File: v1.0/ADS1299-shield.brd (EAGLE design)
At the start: 63.5 x 25.4 mm, 77 parts, among them IC2 TPS72325DBVT, IC3 TPS73225DBVT, U1 ADS1299IPAG

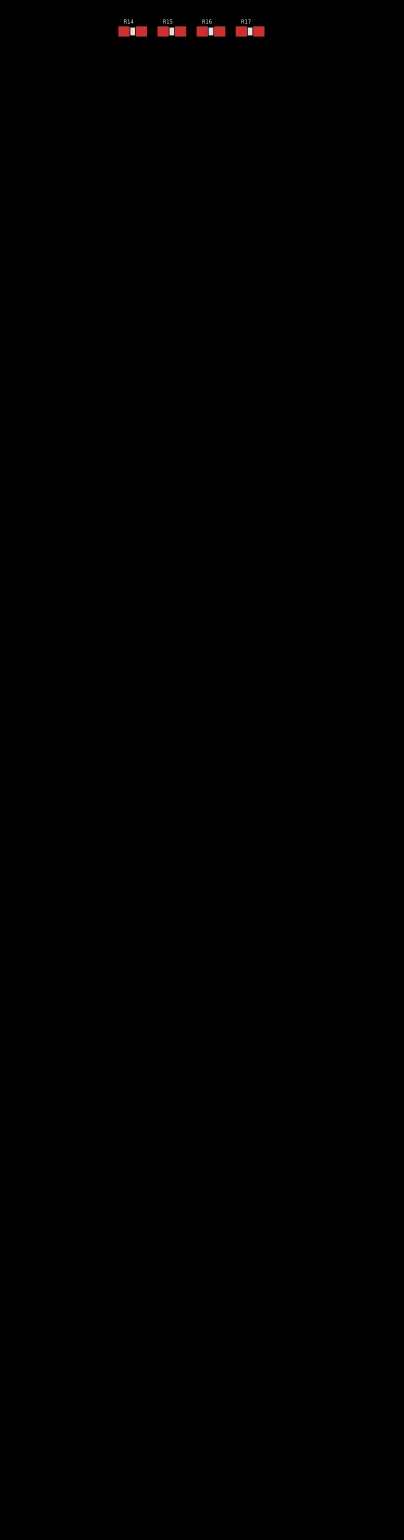
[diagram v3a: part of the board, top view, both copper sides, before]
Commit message: configuration jumpers added but not done; EEPROM in and finished; level shifters finished
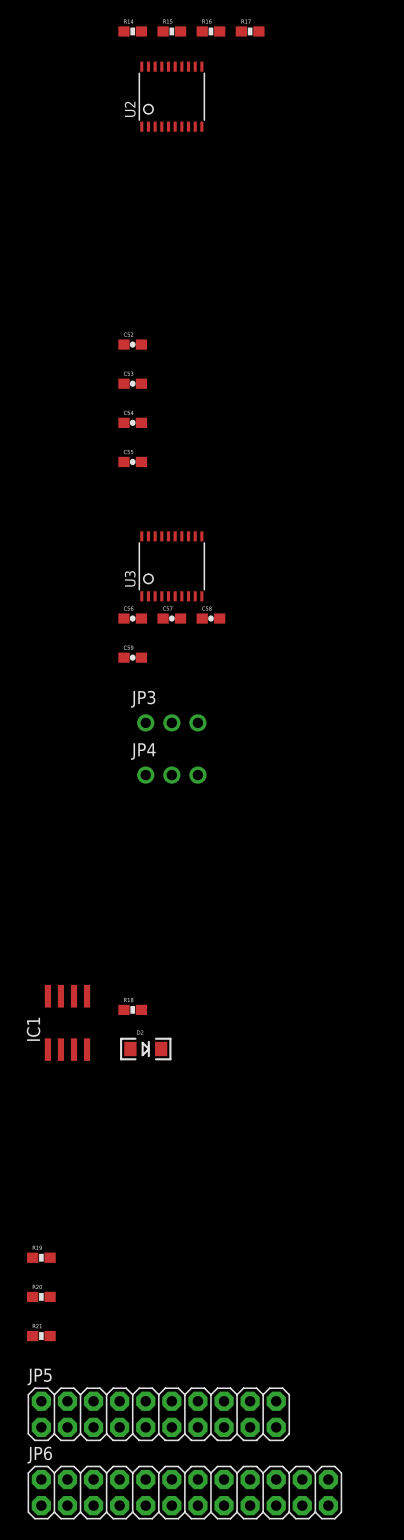
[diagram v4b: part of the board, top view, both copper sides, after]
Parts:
- added C52, C54, C56, C58: 1uF, SparkFun-Passives:0603-CAP
- added C53, C55, C57, C59: 0.1uF, SparkFun-Passives:0603-CAP
- added D2: RED, SparkFun-LED:LED-1206
- added IC1: 24AA256UID, microchip:SO-08
- added JP3, JP4: (no value), adafruit:1X03-CLEANBIG
- added JP5: (no value), pin-headers:2X10
- added JP6: (no value), pin-headers:2X12
- added R18: 270, SparkFun-Passives:0603-RES
- added R19, R20, R21: 10k, SparkFun-Passives:0603-RES
- added U2, U3: TXB0108PWR, adafruit:TSSOP20
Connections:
- removed net SPI_DRDY: U1.47
- removed net SPI_START: U1.38
- new net !ADS_PWDN: U2.12
- new net !ADS_RESET: U3.20
- new net !SPI_CS: U1.39
- new net ADS_CLK: U2.13
- new net ADS_CLKSEL: U2.14
- new net ADS_DRDY: U2.20
- new net ADS_SPI_CLK: U2.17
- new net ADS_SPI_CS: U2.18
- new net ADS_SPI_IN: U2.16
- new net ADS_SPI_OUT: U2.15
- new net ADS_START: U3.18
- new net ARD_UNUSED@1: U3.17
- new net ARD_UNUSED@2: U3.16
- new net ARD_UNUSED@3: U3.15
- new net ARD_UNUSED@4: U3.14
- new net ARD_UNUSED@5: U3.12, U3.13
- new net BOARD_ADDR_0: IC1.1, JP6.23, R19.2
- new net BOARD_ADDR_1: IC1.2, JP6.21, R20.2
- new net BOARD_ADDR_2: IC1.3, R21.2
- new net DRDY: U1.47, U2.1
- new net DVDD1: C56.2, C57.2, U3.2
- new net IOREF: C54.2, C55.2, U2.19
- new net IOREF1: C58.2, C59.2, U3.19
- new net N$14: D2.A, R18.2
- new net SCL1: IC1.6
- new net SDA1: IC1.5
- new net START: U1.38, U3.3
- new net UNUSED@1: U3.4
- new net UNUSED@2: U3.5
- new net UNUSED@3: U3.6, U3.7
- new net UNUSED@4: U3.8
- new net UNUSED@5: U3.9
- net !PWDN: now also U2.9
- net !RESET: now also U3.1
- net AGND: now also C52.1, C53.1, C54.1, C55.1, C56.1, C57.1, C58.1, C59.1, D2.C, IC1.4, IC1.7, R19.1, R20.1, R21.1, U2.11, U3.11
- net CLK: now also U2.8
- net CLKSEL: now also U2.7
- net DVDD: now also C52.2, C53.2, IC1.8, JP6.22, JP6.24, U2.2
- net GPIO4: now also R18.1
- net SPI_CLK: now also U2.4
- net SPI_CS: now also U2.3; no longer U1.39
- net SPI_IN: now also U2.5
- net SPI_OUT: now also U2.6
